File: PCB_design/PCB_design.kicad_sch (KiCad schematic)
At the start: 39 parts, among them J1 USB_B_Micro, J4 Conn_01x02_Pin, Q1 FS8205A, U1 L298N, U2 L7805, U3 TP4056, U4 DW01A

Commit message: Fix errors on circuit schematic and reorder PCB layout
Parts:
- removed A1: Arduino_Nano_v2.x, Module:Arduino_Nano, symbol MCU_Module:Arduino_Nano_v2.x
- added J10, J11, J3, J5, J6, J7, J8: Conn_01x01_Socket, TestPoint:TestPoint_Loop_D1.80mm_Drill1.0mm_Beaded, symbol Connector:Conn_01x01_Socket
- added J2: Conn_01x04_Socket, Connector_Hirose:Hirose_DF13-04P-1.25DSA_1x04_P1.25mm_Vertical, symbol Connector:Conn_01x04_Socket
- C1, C2: value 220uF -> 10uF; footprint Capacitor_220uF35V_smaller:CAPAE1050X1050N -> Capacitor_SMD:C_0603_1608Metric_Pad1.08x0.95mm_HandSolder
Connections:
- net +5V: now also C1.1, R9.1, U1.9 (Vss), U2.3 (OUT), J3.1 (Pin_1)
- net Boost_Out: now also C2.1, D1.1 (K), D3.1 (K), D5.1 (K), D7.1 (K)
- net GND: now also C1.2, J10.1 (Pin_1), J11.1 (Pin_1)
- net OUT1: now also J2.1 (Pin_1)
- net OUT2: now also J2.2 (Pin_2)
- net OUT3: now also J2.3 (Pin_3)
- net OUT4: now also J2.4 (Pin_4)
- net A2: now reaches U1.10 (IN3)
- net A2: now also J7.1 (Pin_1)
- net A3: now reaches U1.12 (IN4)
- net A3: now also J8.1 (Pin_1)
- net A0: now reaches U1.5 (IN1)
- net A0: now also J5.1 (Pin_1)
- net A1: now reaches U1.7 (IN2)
- net A1: now also J6.1 (Pin_1)
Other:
- note added: "1uF"
- note removed: "105"

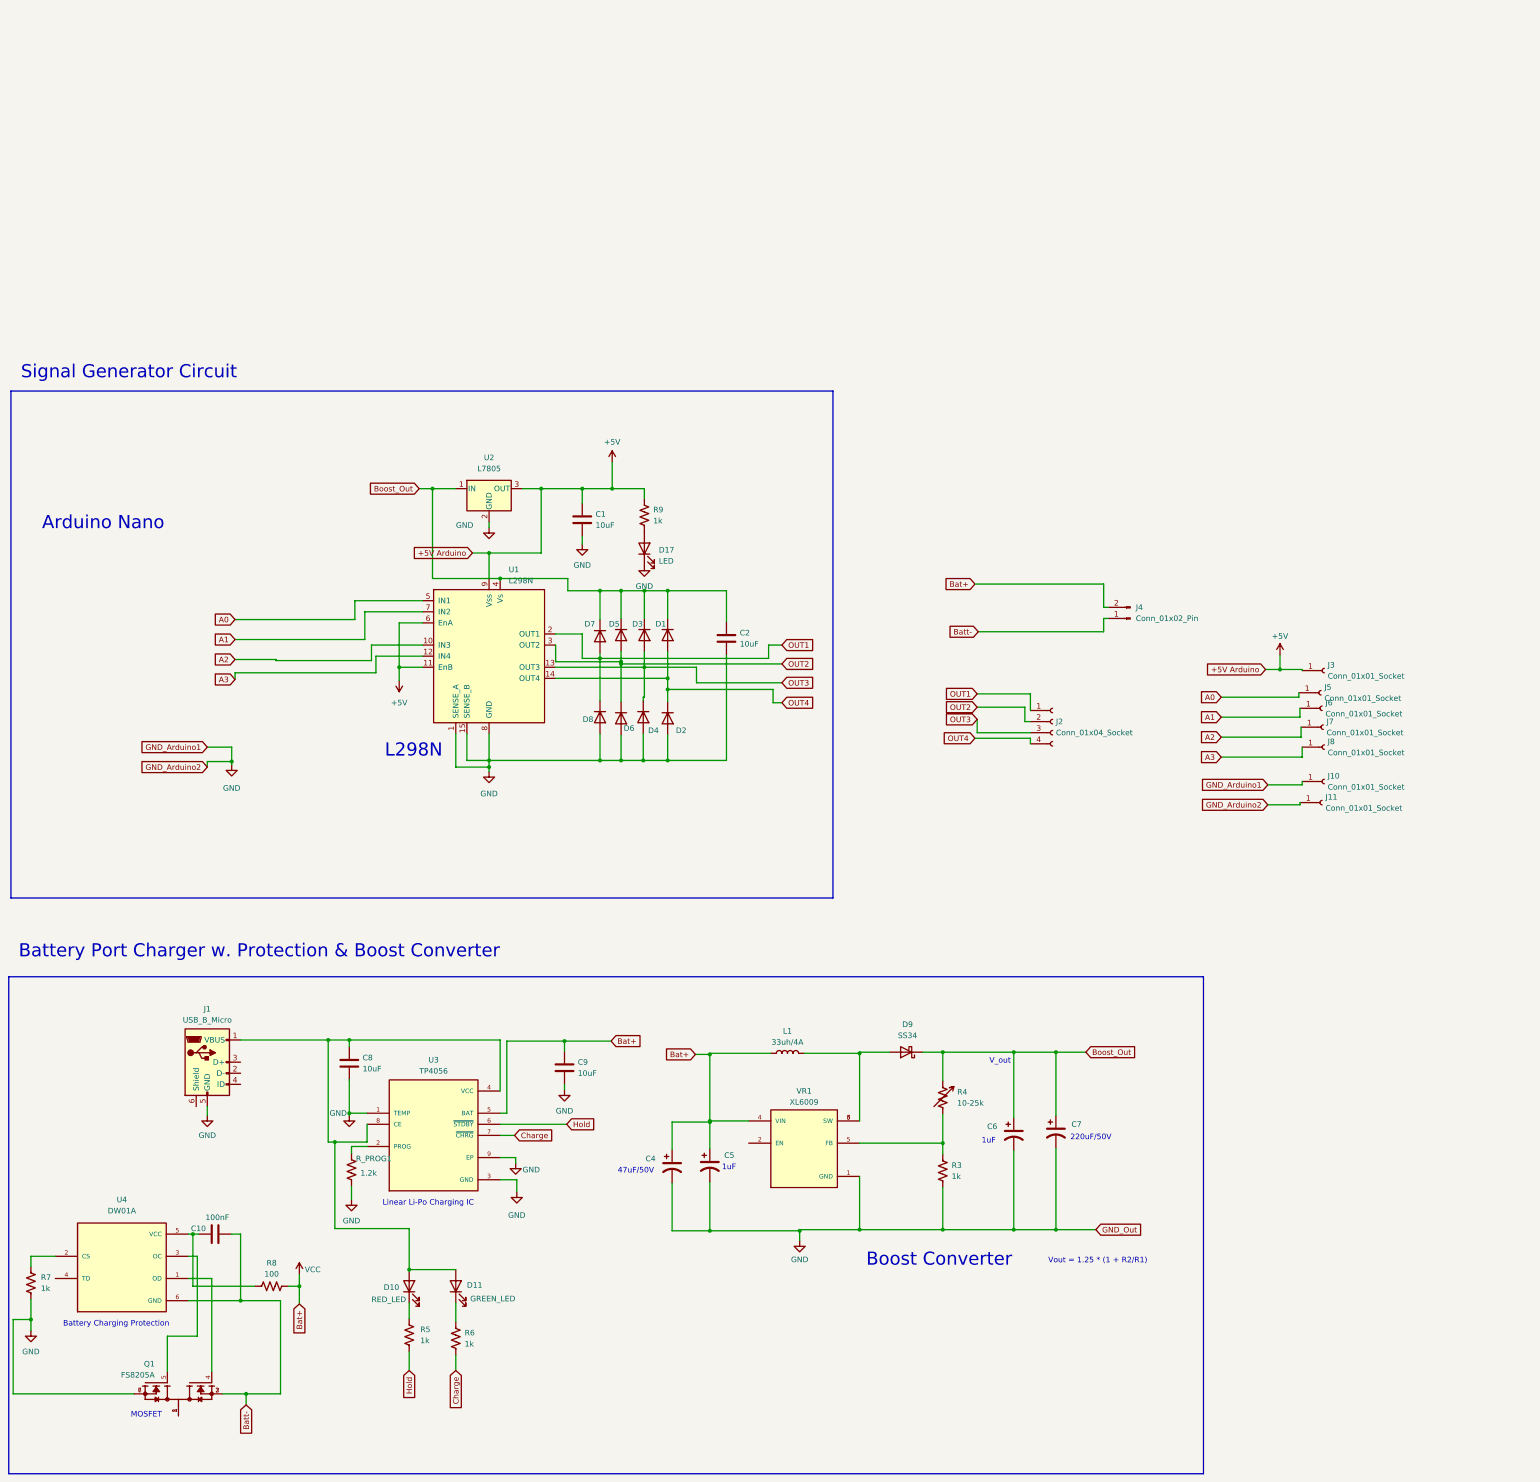
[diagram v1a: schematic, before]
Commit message: Finished PCB design and outline, added interactive html design
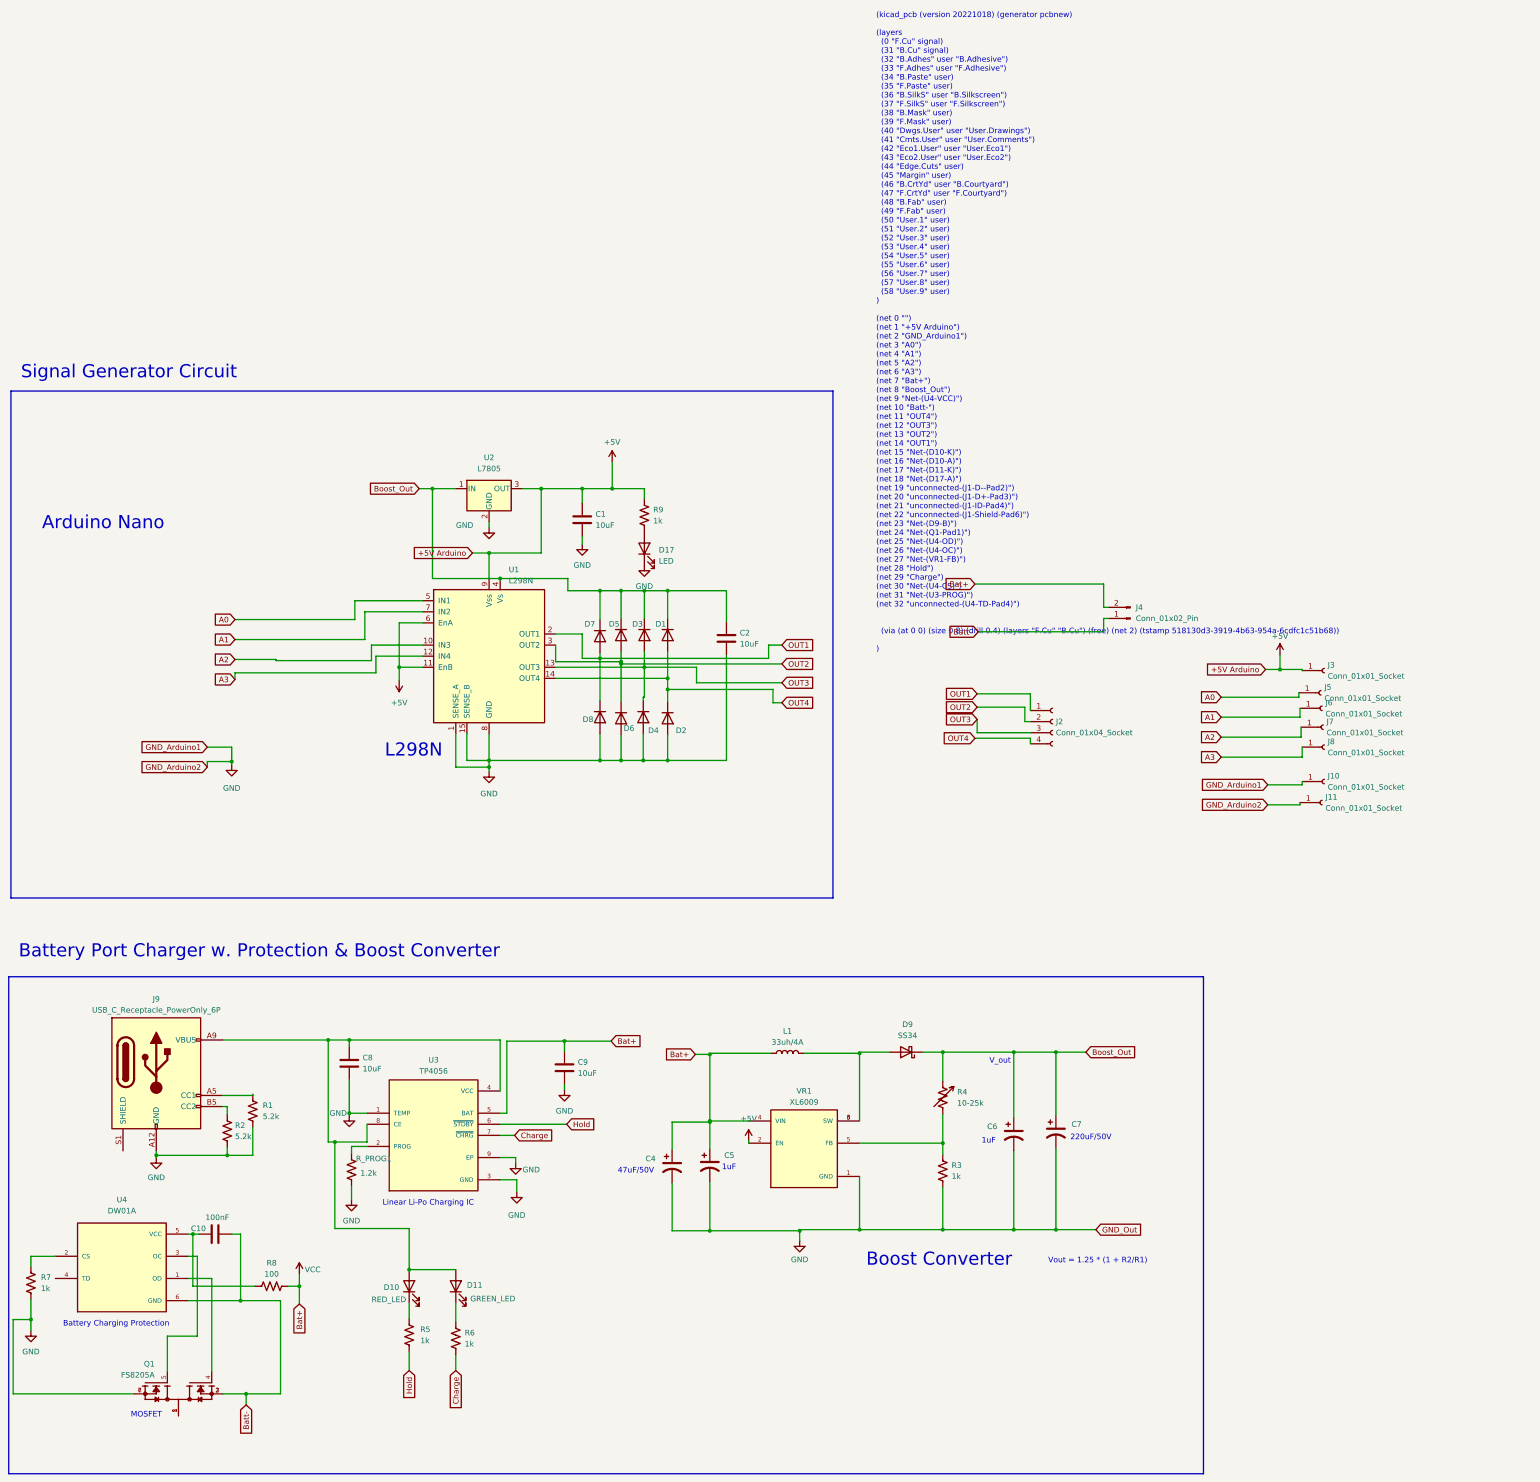
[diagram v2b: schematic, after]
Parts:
- removed J1: USB_B_Micro, Connector_USB:USB_Mini-B_AdamTech_MUSB-B5-S-VT-TSMT-1_SMD_Vertical, symbol Connector:USB_B_Micro
- added J9: USB_C_Receptacle_PowerOnly_6P, Connector_USB:USB_C_Receptacle_GCT_USB4135-GF-A_6P_TopMnt_Horizontal, symbol Connector:USB_C_Receptacle_PowerOnly_6P
- added R1, R2: 5.2k, Resistor_SMD:R_0603_1608Metric_Pad0.98x0.95mm_HandSolder, symbol Device:R_US
- C4: value C_Polarized_US -> 47uF/50V
- C5, C6: value C_Polarized_US -> 1uF
- C7: value C_Polarized_US -> 220uF/50V
- J10, J11, J3, J5, J6, J7, J8: footprint TestPoint:TestPoint_Loop_D1.80mm_Drill1.0mm_Beaded -> TestPoint:TestPoint_THTPad_1.0x1.0mm_Drill0.5mm
- J2: footprint Connector_Hirose:Hirose_DF13-04P-1.25DSA_1x04_P1.25mm_Vertical -> Connector_PinHeader_1.00mm:PinHeader_1x04_P1.00mm_Vertical
- J4: footprint Connector_Hirose:Hirose_DF13-02P-1.25DS_1x02_P1.25mm_Horizontal -> Connector_JST:JST_EH_S2B-EH_1x02_P2.50mm_Horizontal
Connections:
- net +5V: now also VR1.2 (EN)
- net GND: now also J9.A12 (GND), J9.B12 (GND), R1.2, R2.2
- net at C8.1, D10.2 (A), D11.2 (A)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: now also J9.A9 (VBUS), J9.B9 (VBUS)
- new net: J9.A5 (CC1), R1.1
- new net: J9.B5 (CC2), R2.1
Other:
- note added: "(kicad_pcb (version 20221018) (generator pcbnew) (layers (0 "F.Cu" signal) (31 "B.Cu" signal) (32 "B.Adhes" user "B.Adhesive") (33 "F.Adhes" user "F.Adhesive") (34 "B.Paste" user) (35 "F.Paste" user) (36 "B.SilkS" user "B.Silkscreen") (37 "F.SilkS" user "F.Silkscreen") (38 "B.Mask" user) (39 "F.Mask" user) (40 "Dwgs.User" user "User.Drawings") (41 "Cmts.User" user "User.Comments") (42 "Eco1.User"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"

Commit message: Added PCB design pdf
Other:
- note removed: "(kicad_pcb (version 20221018) (generator pcbnew) (layers (0 "F.Cu" signal) (31 "B.Cu" signal) (32 "B.Adhes" user "B.Adhesive") (33 "F.Adhes" user "F.Adhesive") (34 "B.Paste" user) (35 "F.Paste" user) (36 "B.SilkS" user "B.Silkscreen") (37 "F.SilkS" user "F.Silkscreen") (38 "B.Mask" user) (39 "F.Mask" user) (40 "Dwgs.User" user "User.Drawings") (41 "Cmts.User" user "User.Comments") (42 "Eco1.User"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"
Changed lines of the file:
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@@
-    (effects (font (size 1.27 1.27)) (justify left bottom))
-  )
-  (text "(kicad_pcb (version 20221018) (generator pcbnew)\n\n(layers\n  (0 \"F.Cu\" signal)\n  (31 \"B.Cu\" signal)\n  (32 \"B.Adhes\" user \"B.Adhesive\")\n  (33 \"F.Adhes\" user \"F.Adhesive\")\n  (34 \"B.Paste\" user)\n  (35 \"F.Paste\" user)\n  (36 \"B.SilkS\" user \"B.Silkscreen\")\n  (37 \"F.SilkS\" user \"F.Silkscreen\")\n  (38 \"B.Mask\" user)\n  (39 \"F.Mask\" user)\n  (40 \"Dwgs.User\" user \"User.Drawings\")\n  (41 \"Cmts.User\" user \"User.Comments\")\n  (42 \"Eco1.User\" user \"User.Eco1\")\n  (43 \"Eco2.User\" user \"User.Eco2\")\n  (44 \"Edge.Cuts\" user)\n  (45 \"Margin\" user)\n  (46 \"B.CrtYd\" user \"B.Courtyard\")\n  (47 \"F.CrtYd\" user \"F.Courtyard\")\n  (48 \"B.Fab\" user)\n  (49 \"F.Fab\" user)\n  (50 \"User.1\" user)\n  (51 \"User.2\" user)\n  (52 \"User.3\" user)\n  (53 \"User.4\" user)\n  (54 \"User.5\" user)\n  (55 \"User.6\" user)\n  (56 \"User.7\" user)\n  (57 \"User.8\" user)\n  (58 \"User.9\" user)\n)\n\n(net 0 \"\")\n(net 1 \"+5V Arduino\")\n(net 2 \"GND_Arduino1\")\n(net 3 \"A0\")\n(net 4 \"A1\")\n(net 5 \"A2\")\n(net 6 \"A3\")\n(net 7 \"Bat+\")\n(net 8 \"Boost_Out\")\n(net 9 \"Net-(U4-VCC)\")\n(net 10 \"Batt-\")\n(net 11 \"OUT4\")\n(net 12 \"OUT3\")\n(net 13 \"OUT2\")\n(net 14 \"OUT1\")\n(net 15 \"Net-(D10-K)\")\n(net 16 \"Net-(D10-A)\")\n(net 17 \"Net-(D11-K)\")\n(net 18 \"Net-(D17-A)\")\n(net 19 \"unconnected-(J1-D--Pad2)\")\n(net 20 \"unconnected-(J1-D+-Pad3)\")\n(net 21 \"unconnected-(J1-ID-Pad4)\")\n(net 22 \"unconnected-(J1-Shield-Pad6)\")\n(net 23 \"Net-(D9-B)\")\n(net 24 \"Net-(Q1-Pad1)\")\n(net 25 \"Net-(U4-OD)\")\n(net 26 \"Net-(U4-OC)\")\n(net 27 \"Net-(VR1-FB)\")\n(net 28 \"Hold\")\n(net 29 \"Charge\")\n(net 30 \"Net-(U4-CS)\")\n(net 31 \"Net-(U3-PROG)\")\n(net 32 \"unconnected-(U4-TD-Pad4)\")\n\n\n  (via (at 0 0) (size 0.8) (drill 0.4) (layers \"F.Cu\" \"B.Cu\") (free) (net 2))\n\n)"
-    (at 223.012 86.36 0)
     (effects (font (size 1.27 1.27)) (justify left bottom))
   )

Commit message: Added design for in parallel transducer plug in
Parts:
- C8, C9: footprint Capacitor_SMD:C_0201_0603Metric_Pad0.64x0.40mm_HandSolder -> Capacitor_SMD:C_0603_1608Metric_Pad1.08x0.95mm_HandSolder
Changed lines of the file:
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@@
       (effects (font (size 1.27 1.27)) (justify left))
     )
-    (property "Footprint" "Capacitor_SMD:C_0201_0603Metric_Pad0.64x0.40mm_HandSolder" (at 103.3272 184.15 0)
+    (property "Footprint" "Capacitor_SMD:C_0603_1608Metric_Pad1.08x0.95mm_HandSolder" (at 103.3272 184.15 0)
       (effects (font (size 1.27 1.27)) hide)
     )
@@
       (effects (font (size 1.27 1.27)) (justify left))
     )
-    (property "Footprint" "Capacitor_SMD:C_0201_0603Metric_Pad0.64x0.40mm_HandSolder" (at 152.6032 185.166 0)
-      (effects (font (size 1.27 1.27)) hide)
-    )
+    (property "Footprint" "Capacitor_SMD:C_0603_1608Metric_Pad1.08x0.95mm_HandSolder" (at 152.6032 185.166 0)
+      (effects (font (size 1.27 1.27)) hide)
+    )

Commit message: Add new PCB Design
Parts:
- removed Q1: FS8205A, FS8205A:SOP65P640X120-8N, symbol FS8205A:FS8205A
- added Q2: FS8205, FS8205:SOT95P280X145-6N, symbol FS8205:FS8205
- added SW1: SW_SPDT, MINI-SPDT-SW:SW_MINI-SPDT-SW, symbol Switch:SW_SPDT
- C4: footprint Capacitor_220uF35V_smaller:CAPAE1050X1050N -> Capacitor_SMD:CP_Elec_6.3x7.7
- C5: footprint Capacitor_SMD:C_0201_0603Metric_Pad0.64x0.40mm_HandSolder -> Capacitor_SMD:C_0603_1608Metric_Pad1.08x0.95mm_HandSolder
- C7: footprint Capacitor_220uF35V_smaller:CAPAE1050X1050N -> CAP-SMD_BD10.0-L10.3-W10.3-FD:CAP-SMD_BD10.0-L10.3-W10.3-FD
- D1, D2, D3, D4, D5, D6, D7, D8: footprint Diode_SMD:D_0603_1608Metric_Pad1.05x0.95mm_HandSolder -> Diode_SMD:D_0805_2012Metric_Pad1.15x1.40mm_HandSolder
- L1: footprint Inductor_SMD:L_7.3x7.3_H3.5 -> Inductor_SMD:ND-SMD_L11.6-W10.1_final_13mm
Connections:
- net Batt-: now also Q2.3
- net GND: now also Q2.1
- net VCC: now also SW1.1 (A), SW1.2 (B); no longer J4.2 (Pin_2)
- net at U4.1 (OD): now also Q2.4
- net at U4.3 (OC): now also Q2.6
- new net: Q2.2, Q2.5
- new net: J4.2 (Pin_2), SW1.3 (C)
